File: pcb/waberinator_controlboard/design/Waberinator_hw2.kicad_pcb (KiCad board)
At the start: 4 copper layers, 49.5 x 104 mm, 98 parts, among them J1 Conn_01x04_Pin, J27 Conn_01x04, J28 Conn_01x04, J29 Conn_01x04, J4 Conn_01x08_Pin, Q1 AOSP21321, Q2 SISHA04DN-T1-GE3, Q3 SISHA04DN-T1-GE3, Q4 SISHA04DN-T1-GE3, Q5 SISHA04DN-T1-GE3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

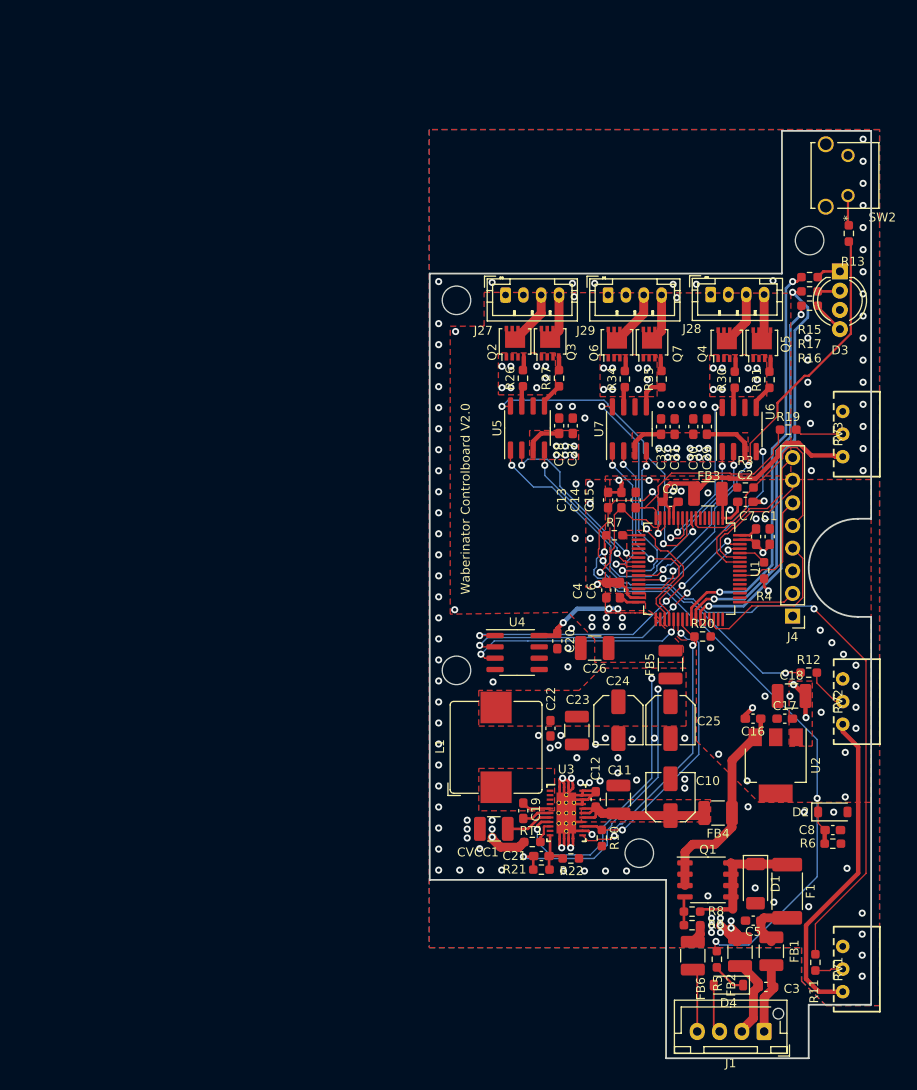
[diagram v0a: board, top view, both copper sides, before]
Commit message: [HW/FW] reshape board to get special offer, reassign some pins
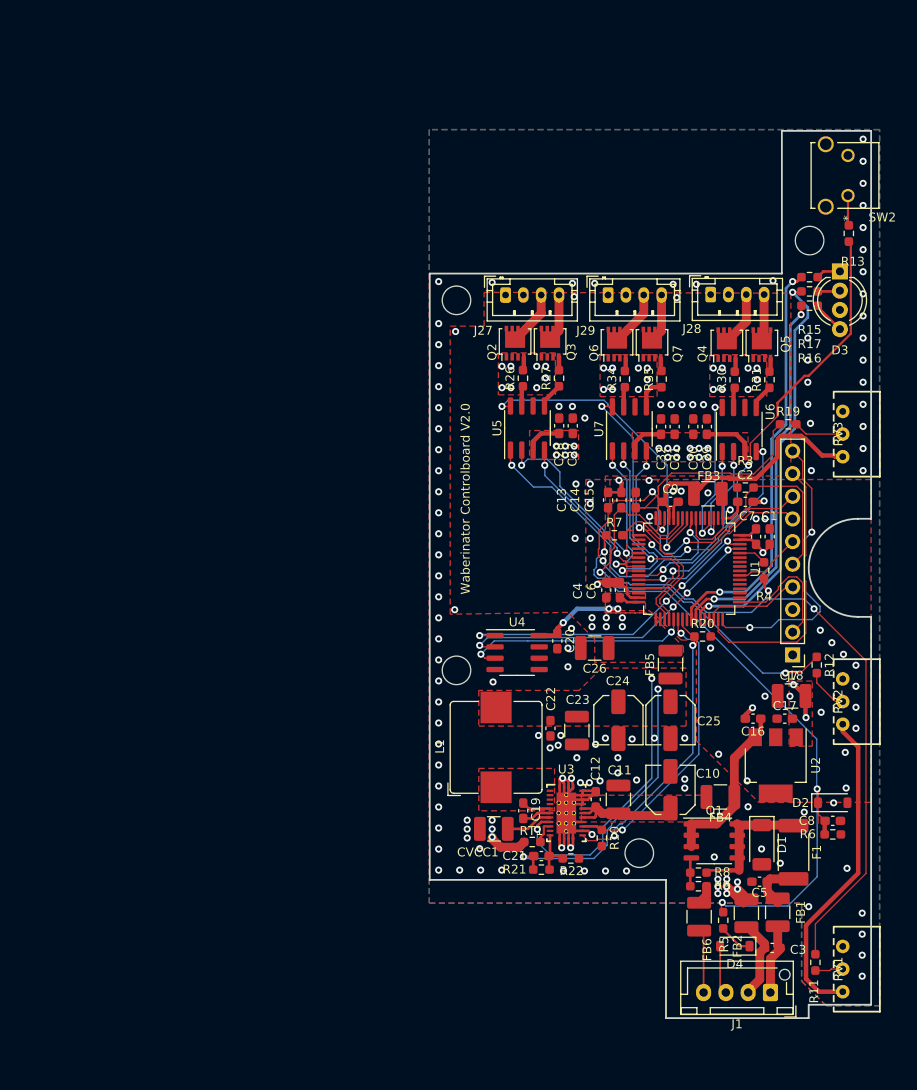
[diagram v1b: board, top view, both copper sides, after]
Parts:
- removed J4: Conn_01x08_Pin, Connector_PinHeader_2.54mm:PinHeader_1x08_P2.54mm_Vertical
- added J7: Conn_01x10_Pin, Connector_PinHeader_2.54mm:PinHeader_1x10_P2.54mm_Vertical, F.Cu at (107.2, 182.3)
- moved C3 4.43 mm to (104.9, 215.1)
- moved D1 4.43 mm to (103.7, 203.6)
- moved D4 4.43 mm to (100.7, 214.9)
- moved F1 4.43 mm to (107.3, 204.4)
- moved FB1 4.43 mm to (105.5, 211.1)
- moved FB2 4.43 mm to (102.0, 211.2)
- moved FB6 4.43 mm to (96.7, 211.6)
- moved J1 4.43 mm to (104.7, 220.1)
- moved Q1 4.43 mm to (98.4, 203.1)
- moved R5 4.43 mm to (99.4, 212.0)
- moved R8 4.43 mm to (96.6, 206.7)
- moved R9 4.43 mm to (96.6, 208.2)
- moved C5 4.43 mm to (103.5, 207.7)
- moved NT2 4.43 mm to (100.7, 206.4)
- moved FB4 1.82 mm to (99.1, 198.2)
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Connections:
- net /lm76606_out renamed /lm73606_out
- U1 pad 10: /ledstring3_drv_en -> /vbat_meas
- U1 pad 11: /ledstring4_drv_en -> /adc_frequency
- U1 pad 15: /adc_frequency -> /adc_depth
- U1 pad 16: /adc_depth -> /usart1_tx_mcu
- U1 pad 17: /vbat_meas -> /usart1_rx_mcu
- U1 pad 3: unconnected-(U1-PC14-Pad3) -> /ledstring3_drv_en
- U1 pad 4: unconnected-(U1-PC15-Pad4) -> /ledstring4_drv_en
- U1 pad 47: unconnected-(U1-PF6-Pad47) -> /spare_1
- U1 pad 48: unconnected-(U1-PF7-Pad48) -> /spare_2
- U1 pad 58: /usart1_tx_mcu -> unconnected-(U1-PB6-Pad58)
- U1 pad 59: /usart1_rx_mcu -> unconnected-(U1-PB7-Pad59)
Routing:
- net /spare_2: track 0.00 -> 32.4 mm, vias 0 -> 2
- net /spare_1: track 0.00 -> 30.7 mm
- net /swd_tck: track 6.33 -> 14.7 mm
- net /vbat_meas: track 2.30 -> 9.89 mm
- net /swd_tms: track 18.3 -> 10.8 mm
- net /usart1_rx_mcu: track 15.3 -> 20.8 mm, vias 0 -> 2
- net /adc_frequency: track 41.6 -> 46.9 mm
- net /ledstring3_drv_en: track 16.3 -> 11.2 mm
- net /swd_swo: track 12.5 -> 7.70 mm
- net /DC_prot: track 23.7 -> 19.2 mm
- net /usart1_tx_mcu: track 18.7 -> 22.9 mm, vias 0 -> 2
- net /lm_vin: track 18.5 -> 14.6 mm
- net /ledstring1_drv_en: track 32.7 -> 34.7 mm
- net +3.3VA: track 107.3 -> 108.7 mm
- net Net-(D2-K): track 74.8 -> 73.4 mm
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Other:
- board size 49.5 x 104 mm -> 49.5 x 99.5 mm

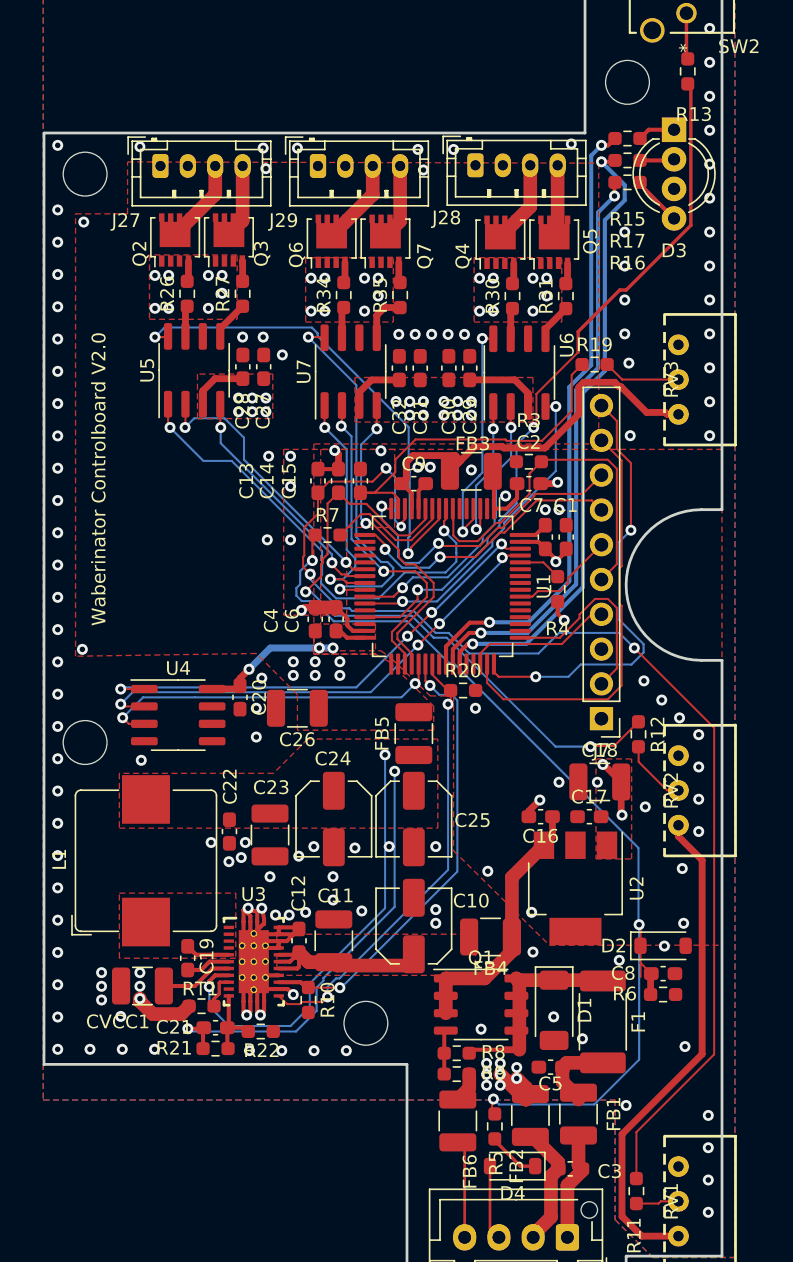
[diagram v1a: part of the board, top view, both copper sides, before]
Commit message: [HW] add esp32
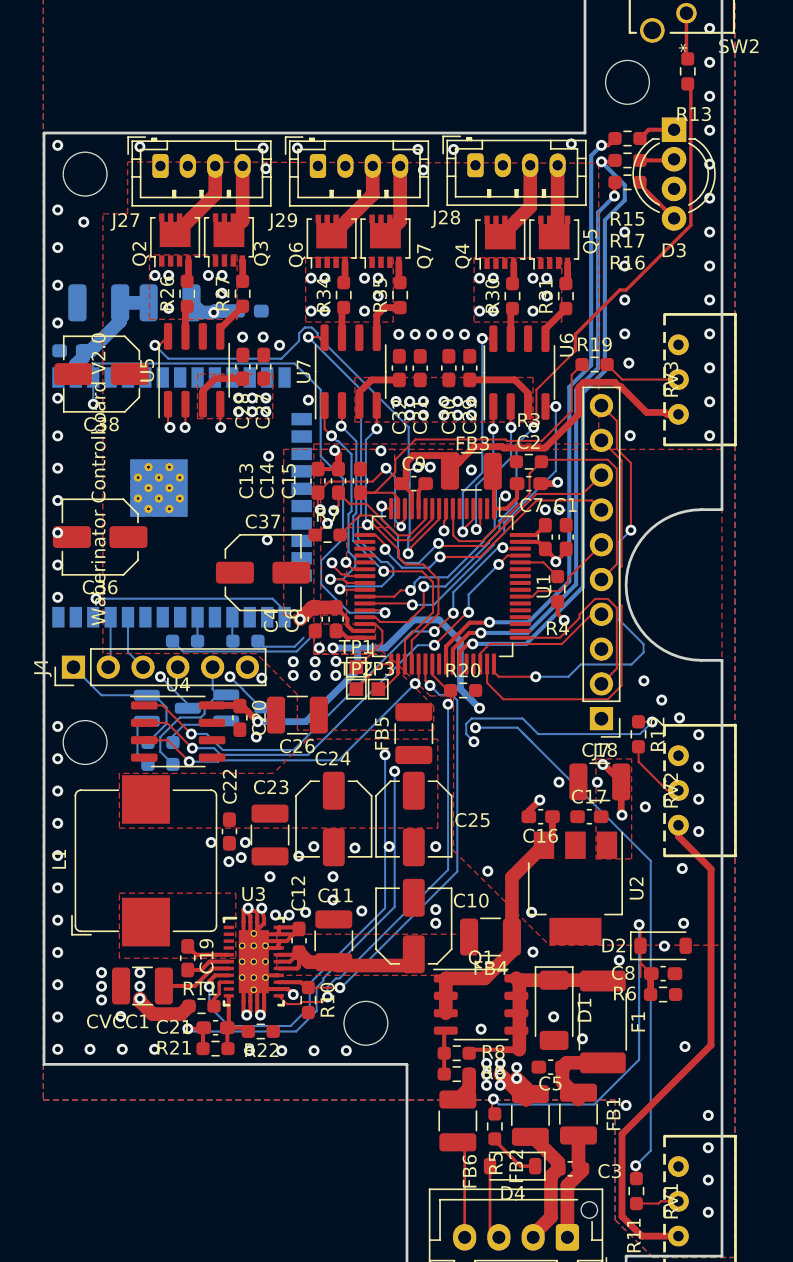
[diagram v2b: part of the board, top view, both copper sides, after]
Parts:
- added C33: 100nF, Capacitor_SMD:C_0603_1608Metric_Pad1.08x0.95mm_HandSolder, B.Cu at (68.5, 155.4)
- added C34: 100µF, Capacitor_SMD:C_1210_3225Metric_Pad1.33x2.70mm_HandSolder, B.Cu at (70.5, 151.9)
- added C35: 100nF, Capacitor_SMD:C_0603_1608Metric_Pad1.08x0.95mm_HandSolder, B.Cu at (81.5, 152.5)
- added C36: 56µF, Capacitor_SMD:C_Elec_5x5.8, F.Cu at (70.6, 169.0)
- added C37: 56µF, Capacitor_SMD:C_Elec_5x5.8, F.Cu at (82.5, 171.6)
- added C38: 56µF, Capacitor_SMD:C_Elec_5x5.8, F.Cu at (70.7, 157.1)
- added FB7: FerriteBead, Capacitor_SMD:C_1210_3225Metric_Pad1.33x2.70mm_HandSolder, B.Cu at (75.7, 151.9)
- added J4: Conn_01x06, Connector_PinHeader_2.54mm:PinHeader_1x06_P2.54mm_Vertical, F.Cu at (68.7, 178.5)
- added Q10: Q_NPN_BEC, Package_TO_SOT_SMD:SOT-23_Handsoldering, B.Cu at (81.3, 181.5)
- added Q8: Q_NPN_BEC, Package_TO_SOT_SMD:SOT-23_Handsoldering, B.Cu at (75.5, 181.5)
- added R1: 100, Resistor_SMD:R_0603_1608Metric_Pad0.98x0.95mm_HandSolder, B.Cu at (81.2, 176.6)
- added R14: 12k, Resistor_SMD:R_0603_1608Metric_Pad0.98x0.95mm_HandSolder, B.Cu at (75.0, 184.0)
- added R18: 12k, Resistor_SMD:R_0603_1608Metric_Pad0.98x0.95mm_HandSolder, B.Cu at (75.0, 185.6)
- added R2: 100, Resistor_SMD:R_0603_1608Metric_Pad0.98x0.95mm_HandSolder, B.Cu at (76.8, 176.6)
- added TP1: TestPoint, TestPoint:TestPoint_Pad_1.0x1.0mm, F.Cu at (89.3, 178.5)
- added TP2: TestPoint, TestPoint:TestPoint_Pad_1.0x1.0mm, F.Cu at (89.3, 180.1)
- added TP3: TestPoint, TestPoint:TestPoint_Pad_1.0x1.0mm, F.Cu at (90.9, 180.1)
- added U8: ESP32-WROOM-32, RF_Module:ESP32-WROOM-32, B.Cu at (75.8, 166.1)
- moved C20 1.50 mm to (80.8, 182.2)
- moved U4 1.20 mm to (76.3, 183.2)
- moved C26 0.50 mm to (85.0, 182.0)
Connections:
- J7 pad 7: /usart1_rx_mcu -> /usart2_rx_mcu
- J7 pad 8: /usart1_tx_mcu -> /usart2_tx_mcu
- U1 pad 16: /usart1_tx_mcu -> /usart2_tx_mcu
- U1 pad 17: /usart1_rx_mcu -> /usart2_rx_mcu
- U1 pad 28: unconnected-(U1-PB2-Pad28) -> /esp32_en
- U1 pad 30: unconnected-(U1-PB11-Pad30) -> /spare_3
- U1 pad 33: unconnected-(U1-PB12-Pad33) -> /spare_4
- U1 pad 34: unconnected-(U1-PB13-Pad34) -> /spare_5
- U1 pad 58: unconnected-(U1-PB6-Pad58) -> /usart1_tx_mcu
- U1 pad 59: unconnected-(U1-PB7-Pad59) -> /usart1_rx_mcu
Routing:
- net /esp32_en: track 0.00 -> 75.2 mm, vias 0 -> 3
- net +3V3: track 20.3 -> 59.3 mm, vias 18 -> 19
- net /esp32_io0: track 0.00 -> 28.2 mm, vias 0 -> 2
- net /usart2_tx_mcu: track 0.00 -> 22.8 mm, vias 0 -> 2
- net /usart2_rx_mcu: track 0.00 -> 20.8 mm, vias 0 -> 2
- net /usart1_rx_mcu: track 20.8 -> 3.89 mm, vias 2 -> 0
- net /adc_brightness: track 89.3 -> 77.1 mm, vias 4 -> 5
- net /usart1_tx_mcu: track 22.9 -> 10.7 mm, vias 2 -> 0
- net /esp32_prog_rts: track 0.00 -> 11.5 mm
- net /esp32_prog_dtr: track 0.00 -> 11.1 mm
- net /esp32_vdd: track 0.00 -> 9.18 mm
- net /ledstring1_drv_en: track 34.7 -> 27.6 mm
- net /spare_3: track 0.00 -> 5.02 mm
- net Net-(Q10-B): track 0.00 -> 4.82 mm
- net /tim3_ch2_ledstring2: track 17.8 -> 22.3 mm
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
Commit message: [HW] finish layout
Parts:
- removed TP3: TestPoint, TestPoint:TestPoint_Pad_1.0x1.0mm
- added R24: 100, Resistor_SMD:R_0603_1608Metric_Pad0.98x0.95mm_HandSolder, B.Cu at (88.4, 182.8)
- moved Q10 0.22 mm to (81.3, 181.7)
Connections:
- U1 pad 34: /spare_5 -> Net-(U1-PB13)
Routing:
- net /usart1_rx_mcu: track 3.89 -> 22.1 mm, vias 0 -> 1
- net /usart1_tx_mcu: track 10.7 -> 28.1 mm, vias 0 -> 1
- net /esp32_io0: track 28.2 -> 42.5 mm
- net /esp32_prog_rts: track 11.5 -> 17.9 mm
- net Net-(U1-PB13): track 0.00 -> 5.47 mm, vias 0 -> 1
- net /spare_2: track 32.4 -> 28.0 mm
- net /i2c1_scl: track 35.2 -> 39.3 mm, vias 4 -> 2
- net /i2c1_sda: track 35.9 -> 39.3 mm, vias 4 -> 2
- net /spare_5: track 2.78 -> 0.00 mm
- net /ledstring2_drv_en: track 38.1 -> 35.8 mm
- net /lm75b_int: track 24.3 -> 26.6 mm
- net /usart2_tx_mcu: track 22.8 -> 21.1 mm
- net /tim15_ch1_ledstring5: track 24.4 -> 25.5 mm
- net /usart2_rx_mcu: track 20.8 -> 20.2 mm
- net Net-(D2-K): track 77.5 -> 76.9 mm
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
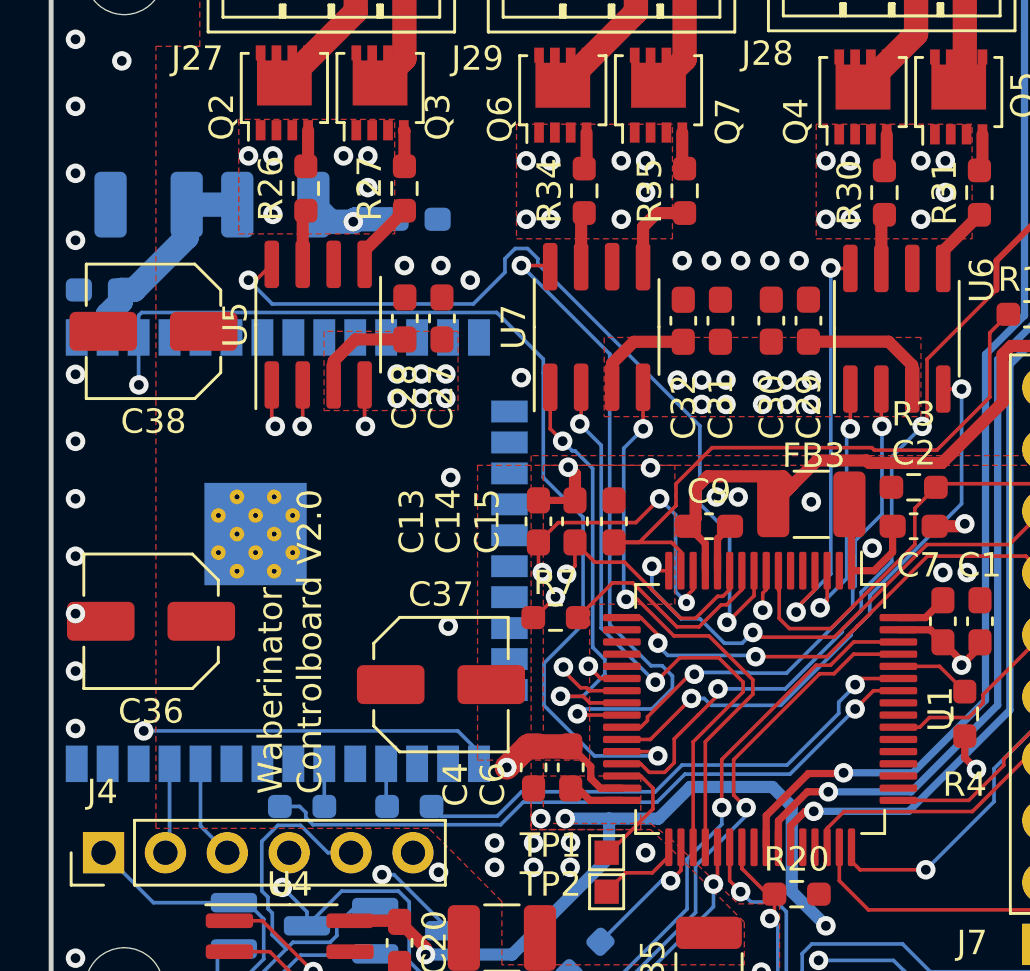
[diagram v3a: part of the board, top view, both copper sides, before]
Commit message: [HW/FW] control power state of modem
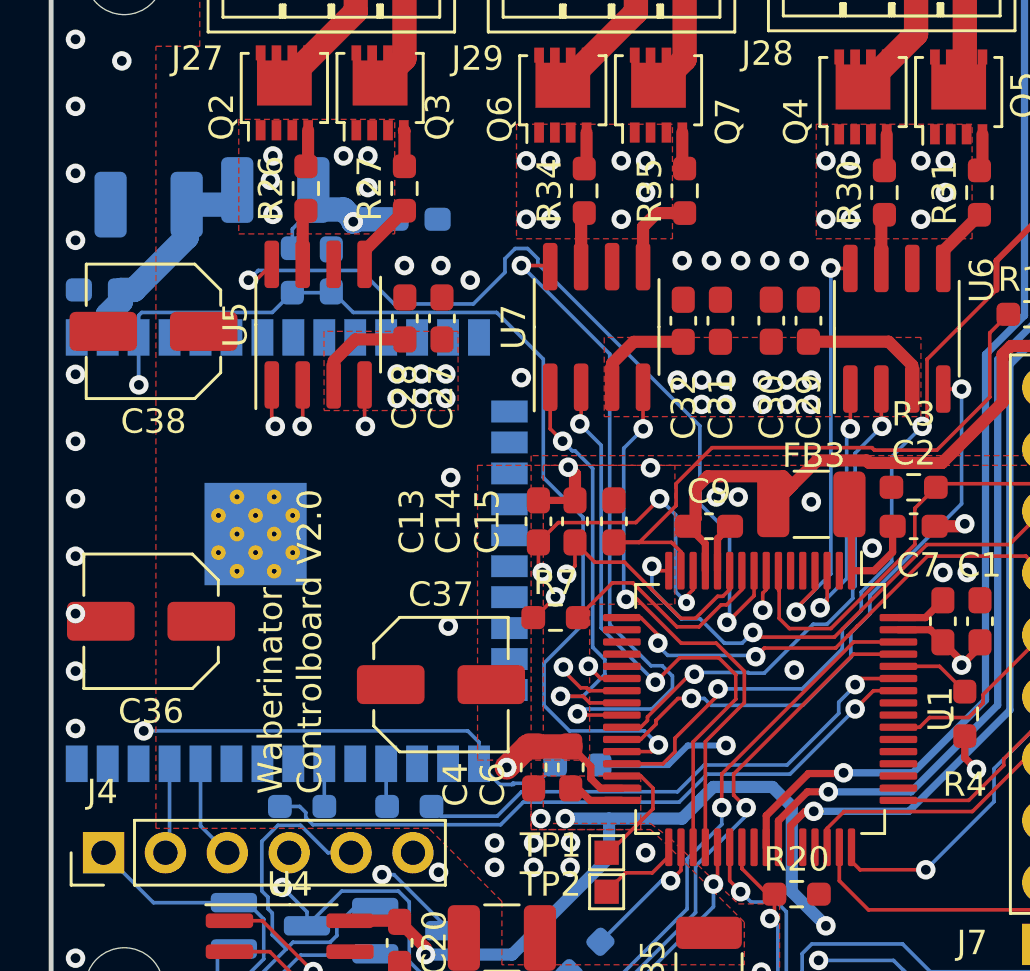
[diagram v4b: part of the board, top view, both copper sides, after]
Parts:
- added C39: 1nF, Capacitor_SMD:C_0603_1608Metric_Pad1.08x0.95mm_HandSolder, B.Cu at (78.0, 154.6)
- added R25: 5k, Resistor_SMD:R_0603_1608Metric_Pad0.98x0.95mm_HandSolder, B.Cu at (88.1, 174.9)
- added R28: 5k, Resistor_SMD:R_0603_1608Metric_Pad0.98x0.95mm_HandSolder, B.Cu at (76.4, 154.6)
- moved FB7 0.60 mm to (75.7, 151.3)
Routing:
- net +3V3: track 59.1 -> 67.4 mm, vias 19 -> 21
- net /esp32_io0: track 42.5 -> 46.6 mm
- net /ledstring1_drv_en: track 27.6 -> 28.5 mm
- net /esp32_en: track 75.5 -> 76.1 mm
- net /tim3_ch4_ledstring4: track 24.1 -> 24.8 mm
